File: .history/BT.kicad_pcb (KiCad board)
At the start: 4 copper layers, 55 x 40 mm, 61 parts, among them J1 Conn_01x05_Pin, J2 Conn_01x03_Pin, J3 Conn_01x06_Pin, J5 Conn_02x03_Odd_Even, K1 AGQ200S12Z, Q1 BSS123, U1 PCM5100A, U2 ESP32-WROOM-32U, U4 AP64060WU-7, U5 AMS1117-3.3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

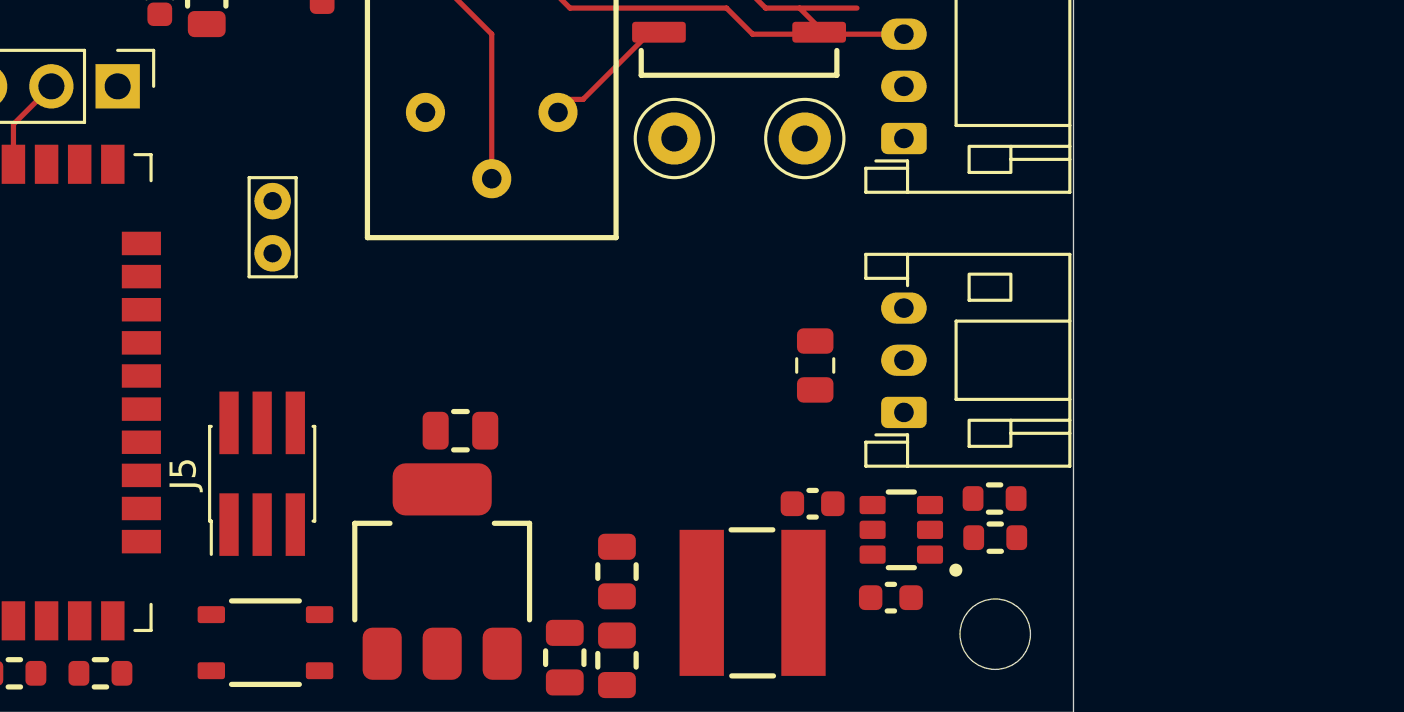
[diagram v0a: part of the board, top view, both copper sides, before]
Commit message: added amplifier. So control volume by knob, signal has to be in injected before the volume control poti. This is why around 5V signal amplitude are necessary.
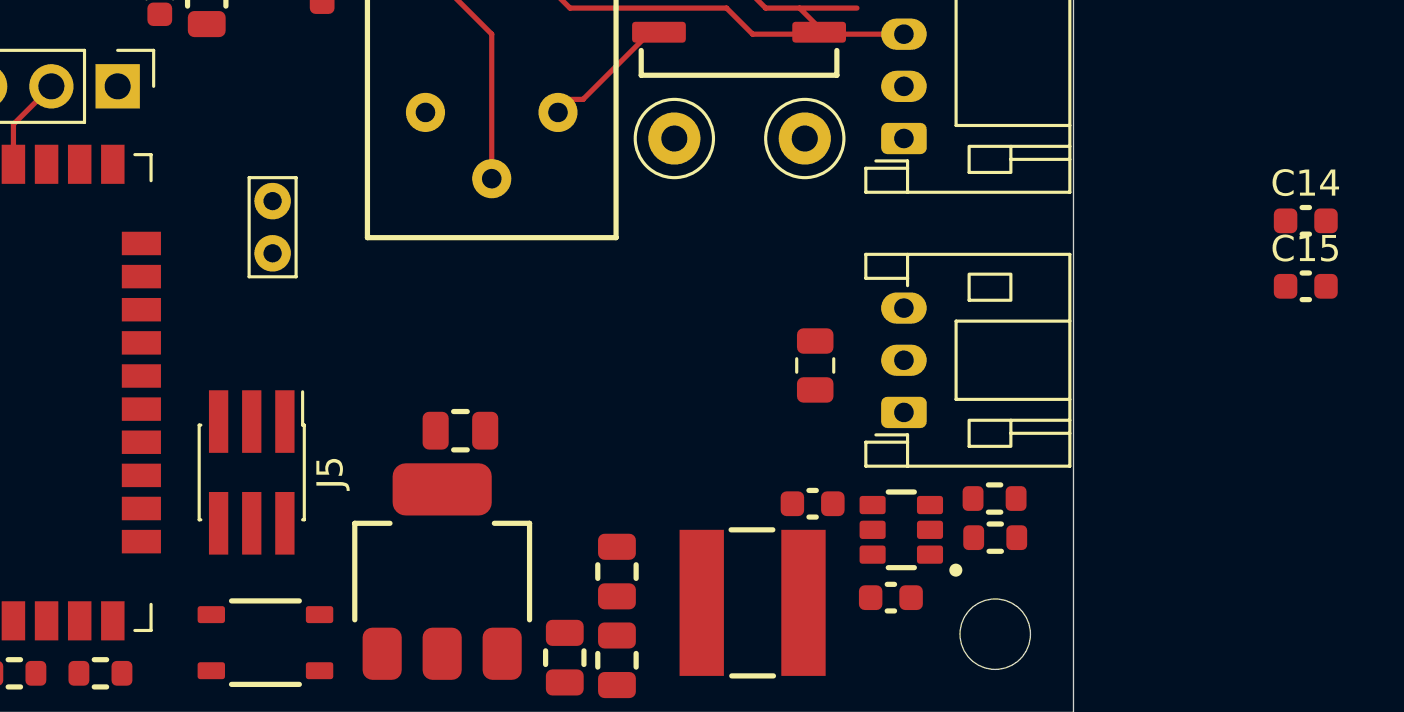
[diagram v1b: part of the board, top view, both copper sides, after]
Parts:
- added C14: 220nF, NRD_CAP:C_0603, F.Cu at (184.6, 96.9)
- added C15: 220nF, NRD_CAP:C_0603, F.Cu at (184.6, 99.4)
- moved J5 0.40 mm to (144.2, 106.5), turned to -90 degrees
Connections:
- C10 pad 1: Net-(U2-EN) -> /ESP_EN
- J5 pad 1: unconnected-(J5-Pin_1-Pad1) -> /ESP_EN
- J5 pad 2: unconnected-(J5-Pin_2-Pad2) -> +3V3
- J5 pad 3: unconnected-(J5-Pin_3-Pad3) -> /ESP_TXD0
- J5 pad 4: unconnected-(J5-Pin_4-Pad4) -> GND
- J5 pad 5: unconnected-(J5-Pin_5-Pad5) -> /ESP_RXD0
- J5 pad 6: unconnected-(J5-Pin_6-Pad6) -> /ESP_IO0
- R2 pad 3: /OUT_L_CON -> Net-(C14-Pad2)
- R3 pad 2: Net-(U2-EN) -> /ESP_EN
- R5 pad 3: /OUT_R_CON -> Net-(C15-Pad2)
- S1 pad 1: unconnected-(S1-Pad1) -> /ESP_EN
- S1 pad 2: unconnected-(S1-Pad2) -> /ESP_EN
- S1 pad 3: unconnected-(S1-Pad3) -> GND
- S1 pad 4: unconnected-(S1-Pad4) -> GND
- TP2 pad 1: /OUT_L_CON -> Net-(C14-Pad2)
- TP3 pad 1: /OUT_R_CON -> Net-(C15-Pad2)
- U2 pad 25: unconnected-(U2-IO0-Pad25) -> /ESP_IO0
- U2 pad 27: /BCK -> /MCLK
- U2 pad 28: /LRCK -> /BCK
- U2 pad 3: Net-(U2-EN) -> /ESP_EN
- U2 pad 30: /DIN -> /LRCK
- U2 pad 31: unconnected-(U2-IO19-Pad31) -> /DIN
- U2 pad 34: /MCLK -> /ESP_RXD0
- U2 pad 35: unconnected-(U2-TXD0/IO1-Pad35) -> /ESP_TXD0
- U6 pad 17: (no net) -> unconnected-(U6-NC-Pad17)
- U6 pad 18: (no net) -> unconnected-(U6-NC-Pad18)
- U6 pad 19: (no net) -> unconnected-(U6-NC-Pad19)
- U6 pad 2: (no net) -> unconnected-(U6-NC-Pad2)

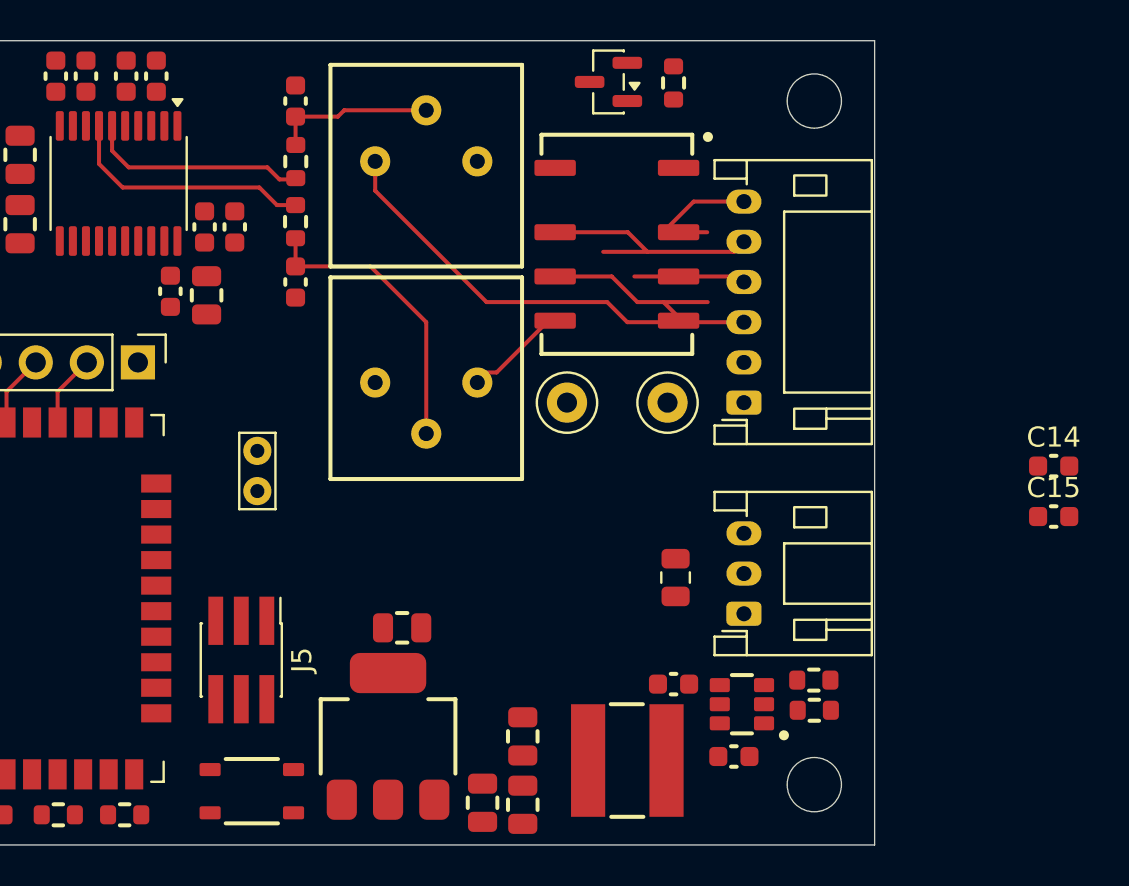
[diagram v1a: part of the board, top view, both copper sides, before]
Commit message: Increased intermediate rail from 5 to 6V; replaced LDO for diigital supply by DCDC
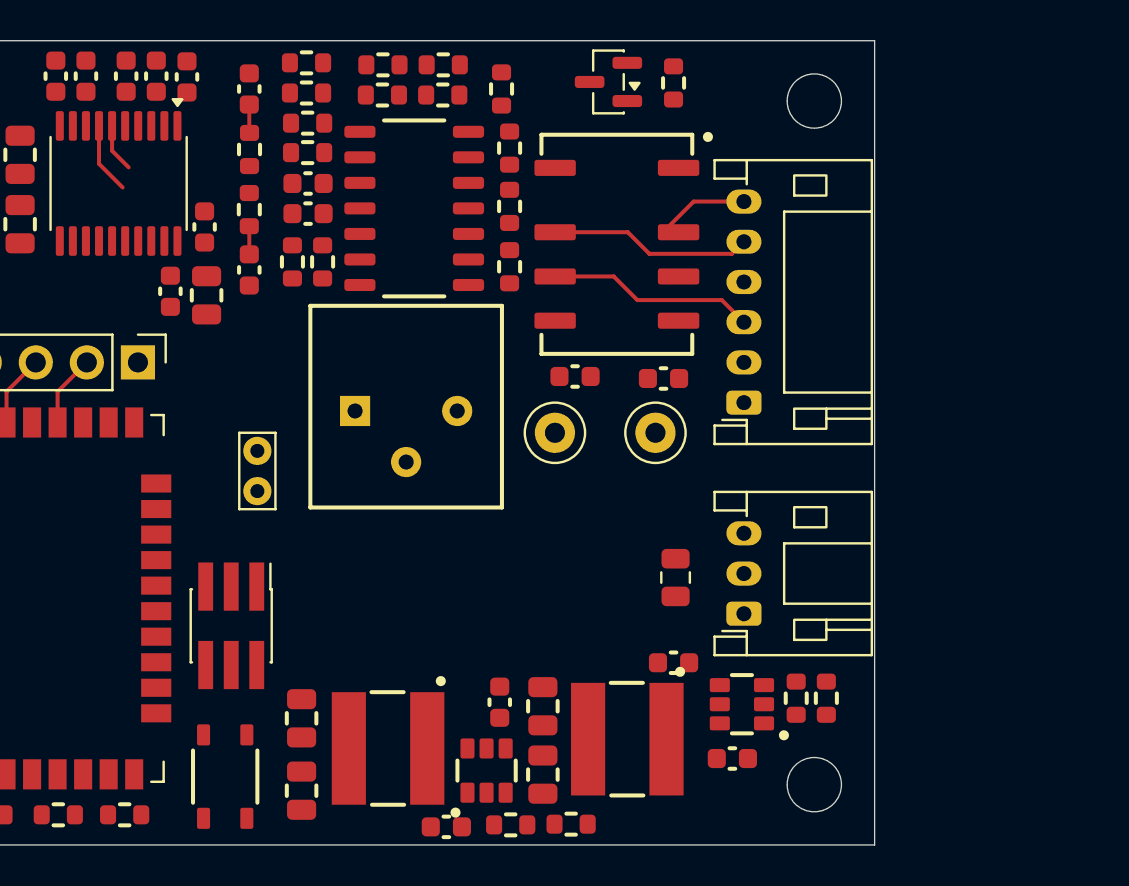
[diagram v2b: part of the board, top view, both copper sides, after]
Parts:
- removed C22, C23: 22uF, NRD_CAP:C_0805
- removed U5: AMS1117-3.3, NRD_LDO:AMS1117
- added C27: 10nF, NRD_CAP:C_0603, F.Cu at (147.5, 84.3)
- added C28: 100nF, NRD_CAP:C_0603, F.Cu at (147.5, 82.8)
- added C29: 2.2uF, NRD_CAP:C_0603, F.Cu at (157.0, 108.6)
- added C30: 100nF, NRD_CAP:C_0603, F.Cu at (154.4, 114.8)
- added C31: 10uF, NRD_CAP:C_0805, F.Cu at (147.2, 113.0)
- added C32: 10uF, NRD_CAP:C_0805, F.Cu at (147.2, 109.4)
- added L2: 8.2uH, NRD_IND:74438367082, F.Cu at (151.5, 110.9)
- added R10: 1M, NRD_RES:R_0603, F.Cu at (147.5, 81.3)
- added R11: 1M, NRD_RES:R_0603, F.Cu at (151.2, 76.9)
- added R12: 1M, NRD_RES:R_0603, F.Cu at (147.4, 76.8)
- added R21: 10K, NRD_RES:R_0603, F.Cu at (147.4, 78.3)
- added R22: 1M, NRD_RES:R_0603, F.Cu at (146.7, 86.7)
- added R23: 1M, NRD_RES:R_0603, F.Cu at (154.2, 76.9)
- added R24: 1M, NRD_RES:R_0603, F.Cu at (148.2, 86.7)
- added R25: 1M, NRD_RES:R_0603, F.Cu at (157.1, 78.1)
- added R26: 10K, NRD_RES:R_0603, F.Cu at (157.5, 87.0)
- added R27: 1M, NRD_RES:R_0603, F.Cu at (151.2, 78.4)
- added R28: 1M, NRD_RES:R_0603, F.Cu at (154.2, 78.4)
- added R29: 1M, NRD_RES:R_0603, F.Cu at (157.5, 84.0)
- added R30: 1M, NRD_RES:R_0603, F.Cu at (157.5, 81.0)
- added R31: 11K5, NRD_RES:R_0603, F.Cu at (160.6, 114.7)
- added R9: 1M, NRD_RES:R_0603, F.Cu at (147.5, 79.8)
- added U3: TLV4888DR, NRD_IC_OPAMP:TLV4888DR, F.Cu at (152.8, 84.0)
- added U7: AP64060WU-7, NRD_IC_DCDC:AP6406x, F.Cu at (156.4, 112.0)
- R18: value 115K -> 2K
- R20: value 22K1 -> 35K7
- R5: value 10K -> 13K; footprint NRD_R_Var:3296P -> NRD_RES:R_0603
- moved R5 25.3 mm to (173.3, 108.4)
- moved C15 24.8 mm to (160.8, 92.4)
- moved C14 19.9 mm to (165.2, 92.5), turned to 180 degrees
- moved R20 16.7 mm to (157.6, 114.7), turned to 0 degrees
- moved R2 12.5 mm to (152.4, 94.1), turned to 90 degrees
- moved C2 7.83 mm to (141.5, 77.5)
- moved R1 2.38 mm to (144.6, 81.1)
- moved C8 2.38 mm to (144.6, 87.1)
- moved C9 2.38 mm to (144.6, 78.1)
- moved R4 2.38 mm to (144.6, 84.1)
- moved C24 1.80 mm to (159.2, 112.2)
- moved C25 1.80 mm to (159.2, 108.8)
- moved J5 1.77 mm to (143.7, 104.8)
- moved TP2 1.62 mm to (164.8, 95.2)
- moved TP3 1.62 mm to (159.8, 95.2)
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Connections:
- net Net-(U4-BST) renamed /BST_+6V
- C24 pad 1: +5V -> +6V
- C25 pad 1: +5V -> +6V
- L1 pad 2: +5V -> +6V
- R18 pad 1: +5V -> /FB_+6V
- R18 pad 2: Net-(U4-FB) -> GND
- R2 pad 1: unconnected-(R2-Pad1) -> Net-(C14-Pad2)
- R2 pad 2: Net-(C9-Pad1) -> GND
- R2 pad 3: Net-(C14-Pad2) -> Net-(R2-Pad3)
- R20 pad 1: Net-(U4-FB) -> +3V3
- R20 pad 2: GND -> /FB_+3V3
- R5 pad 1: unconnected-(R5-Pad1) -> +6V
- R5 pad 2: Net-(C8-Pad1) -> /FB_+6V
- U4 pad 3: Net-(U4-FB) -> /FB_+6V
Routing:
- net /OUT_L_CON: track 19.3 -> 0.11 mm
- net Net-(C8-Pad1): track 14.6 -> 1.40 mm
- net /OUT_R: track 13.0 -> 4.05 mm
- net /OUT_L: track 12.0 -> 3.44 mm
- net Net-(C9-Pad1): track 8.04 -> 1.41 mm
- net /L_OUT: track 5.56 -> 0.39 mm
- net /OUT_R_CON: track 4.94 -> 0.34 mm
- net /R_OUT: track 12.5 -> 10.3 mm
- net /R_IN: track 12.2 -> 10.1 mm
- net /L_IN: track 6.08 -> 4.66 mm

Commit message: clean up
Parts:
- moved R31 0.14 mm to (160.6, 114.8)
- moved R20 0.10 mm to (157.6, 114.8)
- turned C30 to 180 degrees
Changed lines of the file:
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@@
 	(footprint "NRD_RES:R_0603"
 		(layer "F.Cu")
-		(at 160.595 114.675)
+		(at 160.595 114.81)
 		(tags "resistor")
 		(property "Reference" "R31"
@@
 	(footprint "NRD_CAP:C_0603"
 		(layer "F.Cu")
-		(at 154.39 114.81)
+		(at 154.39 114.81 180)
 		(property "Reference" "C30"
 			(at 0 -1.43 0)
@@
 		)
 		(property "Manufacturer" "Samsung"
-			(at 0 0 0)
+			(at 0 0 180)
 			(unlocked yes)
 			(layer "F.Fab")
@@
 		)
 		(property "Manufacturer Part Number" "CL10B104KB8NNNC"
-			(at 0 0 0)
+			(at 0 0 180)
 			(unlocked yes)
 			(layer "F.Fab")
@@
 		)
 		(property "Maximum Operating Temperature [°C]" "125"
-			(at 0 0 0)
+			(at 0 0 180)
 			(unlocked yes)
 			(layer "F.Fab")
@@
 		)
 		(property "Voltage" "50V"
-			(at 0 0 0)
+			(at 0 0 180)
 			(unlocked yes)
 			(layer "F.Fab")
@@
 		)
 		(property "Voltage [V]" "50"
-			(at 0 0 0)
+			(at 0 0 180)
 			(unlocked yes)
 			(layer "F.Fab")
@@
 		)
 		(property "Minimum Operating Temperature [°C]" "-55"
-			(at 0 0 0)
+			(at 0 0 180)
 			(unlocked yes)
 			(layer "F.Fab")
@@
 		)
 		(property "Package" "0603"
-			(at 0 0 0)
+			(at 0 0 180)
 			(unlocked yes)
 			(layer "F.Fab")
@@
 		)
 		(property "RoHS" "Yes"
-			(at 0 0 0)
+			(at 0 0 180)
 			(unlocked yes)
 			(layer "F.Fab")
@@
 		)
 		(property "Tolerance" "±10%"
-			(at 0 0 0)
+			(at 0 0 180)
 			(unlocked yes)
 			(layer "F.Fab")
@@
 		)
 		(property "Tolerance [%]" "10"
-			(at 0 0 0)
+			(at 0 0 180)
 			(unlocked yes)
 			(layer "F.Fab")
@@
 		)
 		(property "Dielectric" "X7R"
-			(at 0 0 0)
+			(at 0 0 180)
 			(unlocked yes)
 			(layer "F.Fab")
@@
 		)
 		(property "Value [F]" "1e-07"
-			(at 0 0 0)
+			(at 0 0 180)
 			(unlocked yes)
 			(layer "F.Fab")
@@
 		(duplicate_pad_numbers_are_jumpers no)
 		(fp_line
-			(start -0.14058 -0.51)
-			(end 0.14058 -0.51)
+			(start -0.14058 0.51)
+			(end 0.14058 0.51)
 			(stroke
 				(width 0.2)
@@
 		)
 		(fp_line
-			(start -0.14058 0.51)
-			(end 0.14058 0.51)
+			(start -0.14058 -0.51)
+			(end 0.14058 -0.51)
 			(stroke
 				(width 0.2)
@@
 		)
 		(pad "1" smd roundrect
-			(at -0.775 0)
+			(at -0.775 0 180)
 			(size 0.9 0.95)
 			(layers "F.Cu" "F.Mask" "F.Paste")
@@
 		)
 		(pad "2" smd roundrect
-			(at 0.775 0)
+			(at 0.775 0 180)
 			(size 0.9 0.95)
 			(layers "F.Cu" "F.Mask" "F.Paste")
@@
 	(footprint "NRD_RES:R_0603"
 		(layer "F.Cu")
-		(at 157.59 114.71)
+		(at 157.59 114.81)
 		(tags "resistor")
 		(property "Reference" "R20"

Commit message: wip
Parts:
- removed C28: 100nF, NRD_CAP:C_0603
- removed J5: Conn_02x03_Odd_Even, Connector_PinHeader_1.27mm:PinHeader_2x03_P1.27mm_Vertical_SMD
- removed L1, L2: 8.2uH, NRD_IND:74438367082
- removed U7: AP64060WU-7, NRD_IC_DCDC:AP6406x
- added C22: 2.2uF, NRD_CAP:C_0805, F.Cu at (182.1, 89.5)
- added C23: 4.7uF, NRD_CAP:C_1206, F.Cu at (196.0, 89.7)
- added C33: 2.2uF, NRD_CAP:C_0805, F.Cu at (182.1, 92.5)
- added C34: 2.2uF, NRD_CAP:C_0805, F.Cu at (182.1, 95.5)
- added C35: 100nF, NRD_CAP:C_0603, F.Cu at (181.9, 101.3)
- added C36: 2.2uF, NRD_CAP:C_0805, F.Cu at (182.1, 98.5)
- added FB2: 4k7@100MHz, Inductor_SMD:L_0805_2012Metric, F.Cu at (195.5, 92.7)
- added FB4: 4k7@100MHz, Inductor_SMD:L_0805_2012Metric, F.Cu at (195.5, 95.5)
- added J4: Boxed_Header_02x03_SMT, NRD_CON:Boxed_Header_02x03_SMT, F.Cu at (145.0, 102.2)
- added R32: 13K7, NRD_RES:R_0603, F.Cu at (181.9, 103.8)
- added RV1: 10K, Potentiometer_SMD:Potentiometer_Bourns_TC33X_Vertical, F.Cu at (152.8, 90.8)
- added U5: TLVM23615RDNR, NRD_IC_DCDC:TxxM336x5, F.Cu at (187.5, 103.1)
- C11, C7: footprint NRD_CAP:C_0603 -> NRD_CAP:C_0805
- C14, C15: value 220nF -> 2.2uF; footprint NRD_CAP:C_0603 -> NRD_CAP:C_0805
- C17: value 100nF -> 4.7uF; footprint NRD_CAP:C_0603 -> NRD_CAP:C_1206
- C18: value 2.2uF -> 100nF
- C19: value 10uF -> 4.7uF; footprint NRD_CAP:C_0805 -> NRD_CAP:C_1206
- C20: value 22uF -> 100nF; footprint NRD_CAP:C_0805 -> NRD_CAP:C_0603
- C21: value 22uF -> 4.7uF; footprint NRD_CAP:C_0805 -> NRD_CAP:C_1206
- C24, C25: value 10uF -> 22uF; footprint NRD_CAP:C_0805 -> NRD_CAP:C_1206
- C26: value 1uF -> 4.7uF; footprint NRD_CAP:C_0603 -> NRD_CAP:C_1206
- C29: value 2.2uF -> 22uF; footprint NRD_CAP:C_0603 -> NRD_CAP:C_1206
- C30: value 100nF -> 22uF; footprint NRD_CAP:C_0603 -> NRD_CAP:C_1206
- C31, C32: value 10uF -> 100nF; footprint NRD_CAP:C_0805 -> NRD_CAP:C_0603
- J3: value Conn_01x06_Pin -> S6B-PH-K-S; footprint Connector_JST:JST_PH_S6B-PH-K_1x06_P2.00mm_Horizontal -> NRD_CON:S6B-PH-K-S
- Q1: footprint Package_TO_SOT_SMD:SOT-23 -> NRD_MOSFET:BSS123
- R17, R19: value 0R -> 10K
- R18: value 2K -> 10K
- R2: value 10K -> 34K; footprint NRD_R_Var:3296P -> NRD_RES:R_0603
- R20: value 35K7 -> 2K
- R31: value 11K5 -> 21K
- R5: value 13K -> 14K3
- U1: footprint Package_SO:TSSOP-20_4.4x6.5mm_P0.65mm -> NRD_IC_DATA:PCM510xx
- U2: footprint RF_Module:ESP32-WROOM-32U -> NRD_IC_MCU:WROOM_32U
- U4: value AP64060WU-7 -> TLVM23615RDNR; footprint NRD_IC_DCDC:AP6406x -> NRD_IC_DCDC:TxxM336x5
- U6: value TPS7A4701 -> RAA214220; footprint NRD_LDO:TPS7A47x -> NRD_LDO:RAA214220
- moved C11 178.1 mm to (311.1, 121.3), turned to 0 degrees
- moved C7 176.0 mm to (311.1, 118.8), turned to 0 degrees
- moved C13 175.6 mm to (315.3, 119.0), turned to 0 degrees
- moved C12 174.1 mm to (311.1, 123.8), turned to 0 degrees
- moved R2 37.7 mm to (186.4, 110.4)
- moved J3 5.55 mm to (171.6, 88.7)
- moved TP1 4.10 mm to (145.2, 92.0)
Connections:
- C17 pad 1: /BST_+6V -> +12V
- C17 pad 2: Net-(U4-SW) -> GND
- C18 pad 1: Net-(U4-EN) -> +12V
- C19 pad 1: +5V -> +12V
- C20 pad 1: +3.3VA -> +12V
- C21 pad 1: +3.3VA -> Net-(U6-VOUT)
- C24 pad 1: +6V -> +3V3
- C25 pad 1: +6V -> +3V3
- C26 pad 1: Net-(U6-NR) -> Net-(U5-VCC)
- C27 pad 1: +5V -> Net-(U3E-V+)
- C30 pad 1: /BST_+3V3 -> +6V
- C30 pad 2: Net-(U7-SW) -> GND
- C32 pad 1: +3V3 -> Net-(C32-Pad1)
- F1 pad 1: Net-(U4-EN) -> +12V
- F1 pad 2: +12V -> /KL30
- J3 pad 1: +12V -> /KL30
- R17 pad 1: Net-(U6-0.1V) -> +6V
- R17 pad 2: GND -> Net-(U5-FB)
- R18 pad 1: /FB_+6V -> Net-(U4-RT)
- R19 pad 1: Net-(U6-3.2V) -> Net-(U5-RT)
- R2 pad 1: Net-(C14-Pad2) -> +3V3
- R2 pad 2: GND -> Net-(U4-FB)
- R20 pad 1: +3V3 -> Net-(U5-FB)
- R20 pad 2: /FB_+3V3 -> GND
- R25 pad 1: Net-(R2-Pad3) -> Net-(R25-Pad1)
- R26 pad 2: Net-(R2-Pad3) -> Net-(R25-Pad1)
- R29 pad 2: Net-(R2-Pad3) -> Net-(R25-Pad1)
- R31 pad 1: /FB_+3V3 -> Net-(U6-VOUT)
- R31 pad 2: GND -> Net-(U6-ADJ)
- R5 pad 1: +6V -> Net-(U4-FB)
- R5 pad 2: /FB_+6V -> GND
- U3 pad 4: +5V -> Net-(U3E-V+)
- U4 pad 1: /BST_+6V -> unconnected-(U4-PGOOD-Pad1)
- U4 pad 2: GND -> +12V
- U4 pad 3: /FB_+6V -> +12V
- U4 pad 4: Net-(U4-EN) -> +3V3
- U4 pad 5: Net-(U4-EN) -> unconnected-(U4-SW-Pad5)_4
- U4 pad 6: Net-(U4-SW) -> unconnected-(U4-SW_2-Pad6)
- U6 pad 1: +3.3VA -> +3V3
- U6 pad 2: unconnected-(U6-NC-Pad2) -> GND
- U6 pad 3: +3.3VA -> +3V3
- U6 pad 4: unconnected-(U6-6.4V-Pad4) -> Net-(U6-ADJ)
- U6 pad 5: unconnected-(U6-6.4V-Pad5) -> Net-(U6-VOUT)
